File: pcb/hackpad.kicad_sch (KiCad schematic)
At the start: 31 parts, among them U1 XIAO-RP2040-SMD

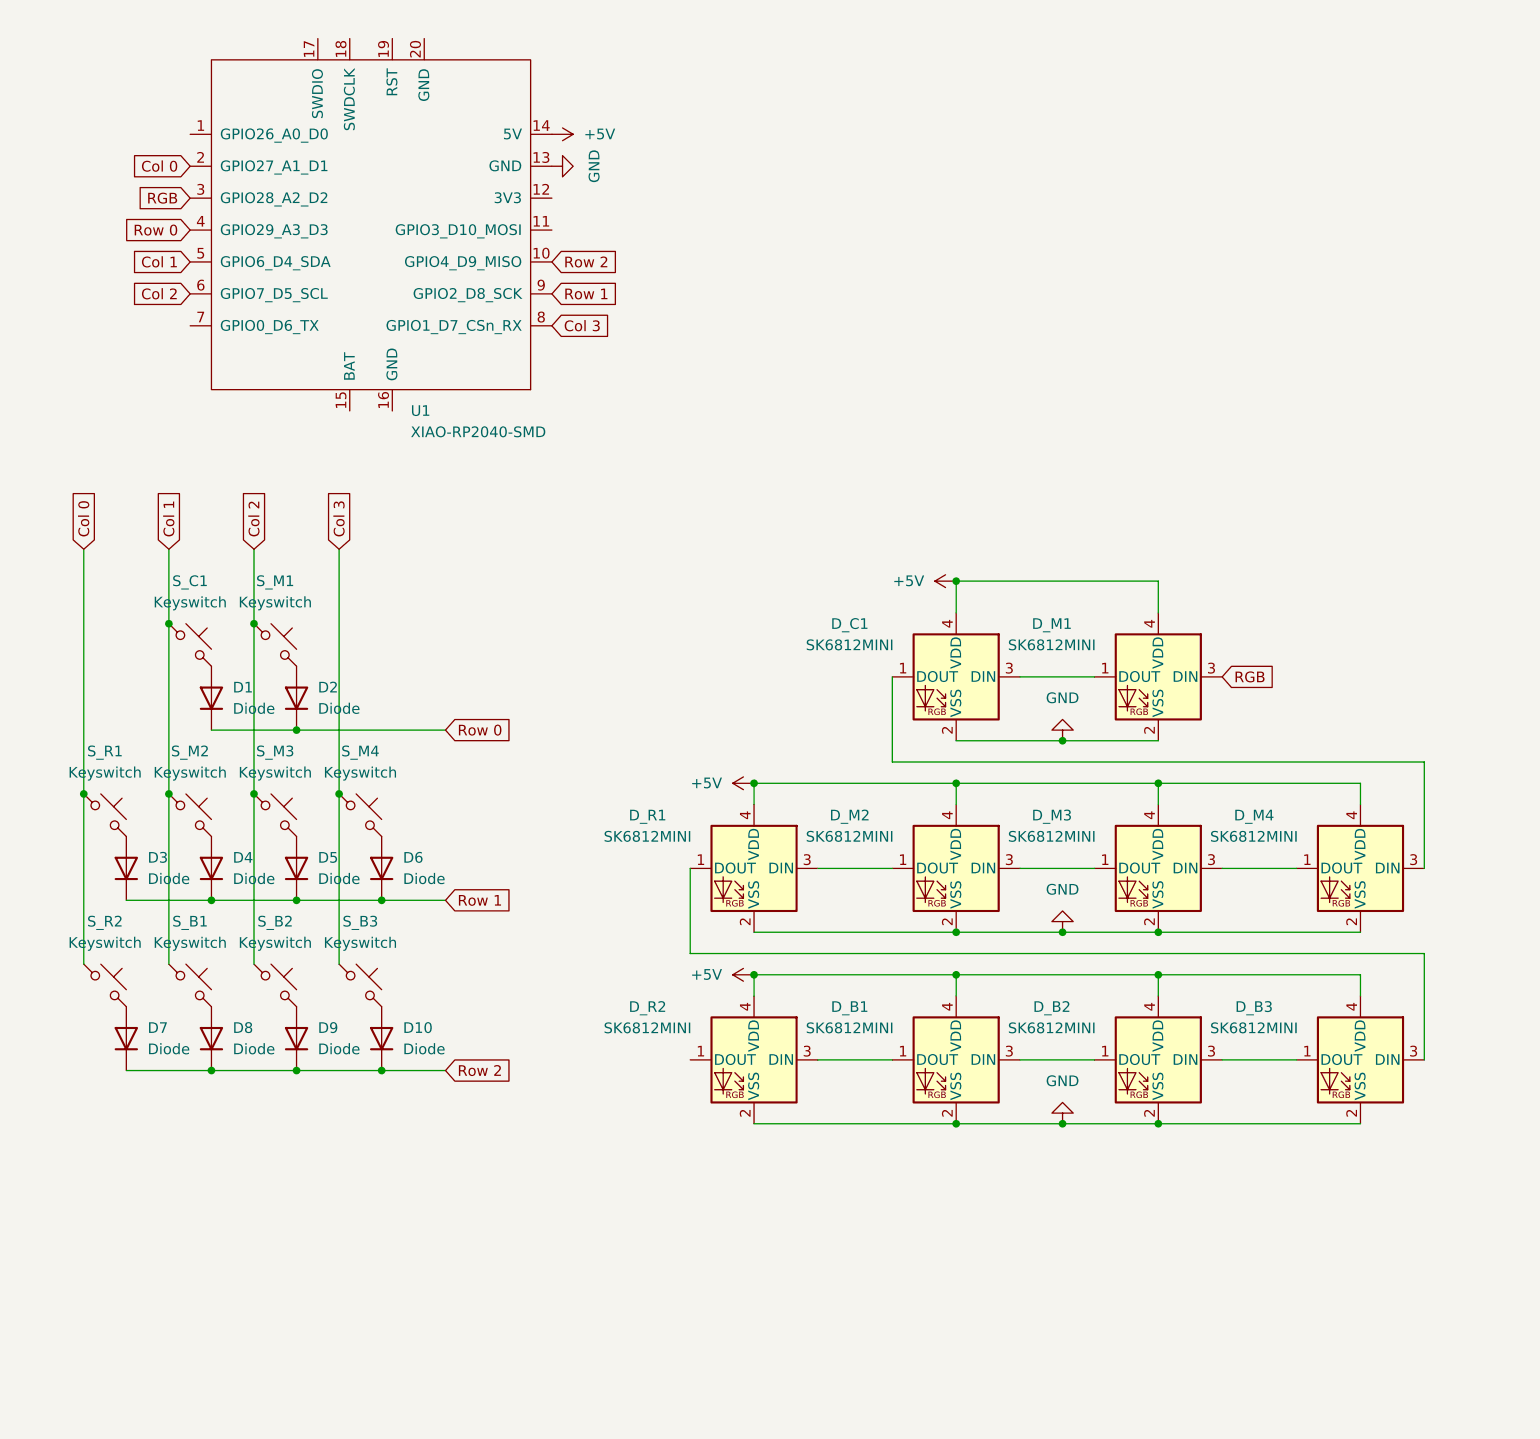
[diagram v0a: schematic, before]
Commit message: i used the wrong data sheet to edit the footprint, changed the pcb to actually work :(
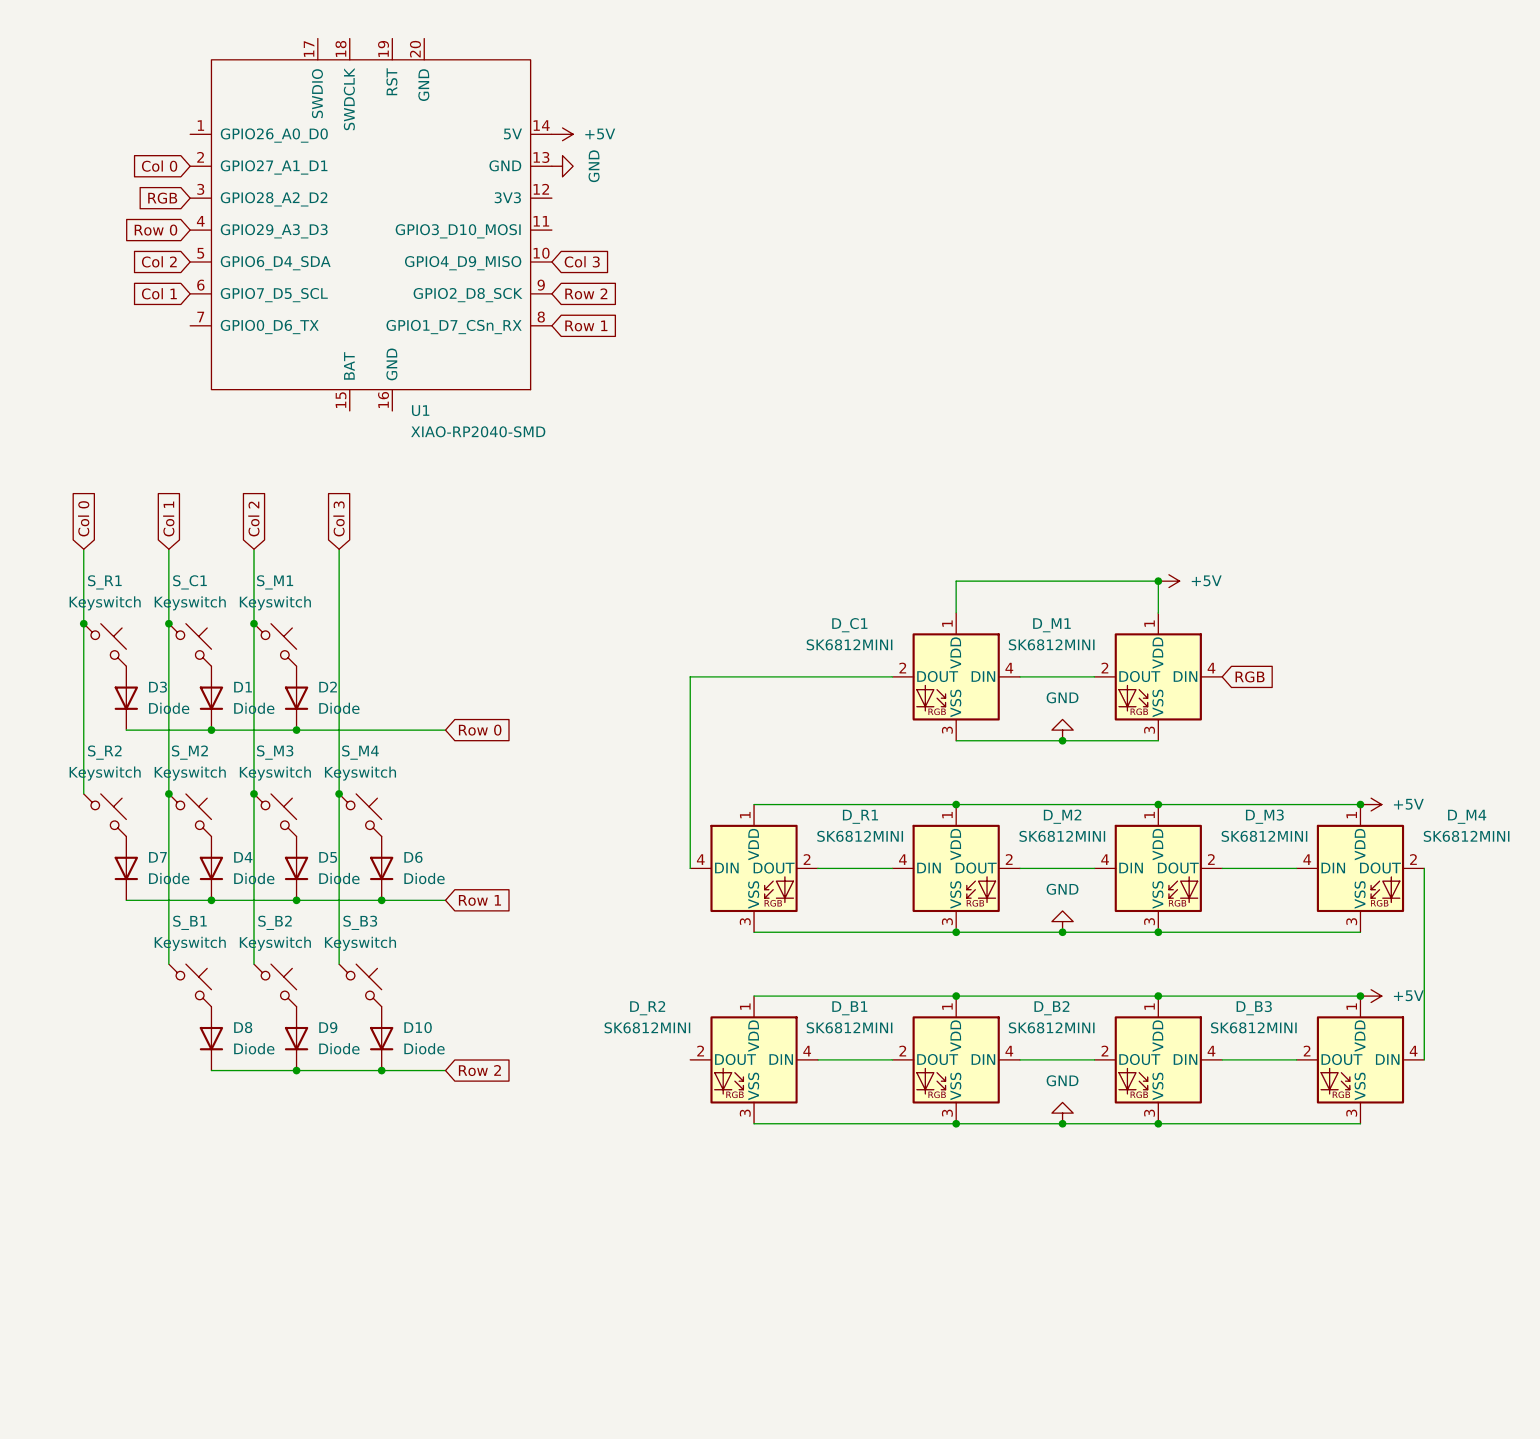
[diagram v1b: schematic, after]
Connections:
- net +5V: now also D_B1.1 (VDD), D_B2.1 (VDD), D_B3.1 (VDD), D_C1.1 (VDD), D_M1.1 (VDD), D_M2.1 (VDD), D_M3.1 (VDD), D_M4.1 (VDD), D_R1.1 (VDD), D_R2.1 (VDD); no longer D_B1.4 (VDD), D_B2.4 (VDD), D_B3.4 (VDD), D_C1.4 (VDD), D_M1.4 (VDD), D_M2.4 (VDD), D_M3.4 (VDD), D_M4.4 (VDD), D_R1.4 (VDD), D_R2.4 (VDD)
- net Col 1: now also U1.6 (GPIO7_D5_SCL); no longer U1.5 (GPIO6_D4_SDA)
- net Col 2: now also U1.5 (GPIO6_D4_SDA); no longer U1.6 (GPIO7_D5_SCL)
- net Col 3: now also U1.10 (GPIO4_D9_MISO); no longer U1.8 (GPIO1_D7_CSn_RX)
- net GND: now also D_B1.3 (VSS), D_B2.3 (VSS), D_B3.3 (VSS), D_C1.3 (VSS), D_M1.3 (VSS), D_M2.3 (VSS), D_M3.3 (VSS), D_M4.3 (VSS), D_R1.3 (VSS), D_R2.3 (VSS); no longer D_B1.2 (VSS), D_B2.2 (VSS), D_B3.2 (VSS), D_C1.2 (VSS), D_M1.2 (VSS), D_M2.2 (VSS), D_M3.2 (VSS), D_M4.2 (VSS), D_R1.2 (VSS), D_R2.2 (VSS)
- net RGB: now also D_M1.4 (DIN); no longer D_M1.3 (DIN)
- net Row 0: now also D3.1 (K)
- net Row 1: now also D7.1 (K), U1.8 (GPIO1_D7_CSn_RX); no longer D3.1 (K), U1.9 (GPIO2_D8_SCK)
- net Row 2: now also U1.9 (GPIO2_D8_SCK); no longer D7.1 (K), U1.10 (GPIO4_D9_MISO)
- new net: D_C1.4 (DIN), D_M1.2 (DOUT)
- new net: D_B2.4 (DIN), D_B3.2 (DOUT)
- new net: D_B3.4 (DIN), D_M4.2 (DOUT)
- new net: D_B1.4 (DIN), D_B2.2 (DOUT)
- new net: D_B1.2 (DOUT), D_R2.4 (DIN)
- new net: D_M2.4 (DIN), D_R1.2 (DOUT)
- new net: D_C1.2 (DOUT), D_R1.4 (DIN)
- new net: D_M3.2 (DOUT), D_M4.4 (DIN)
- new net: D_M2.2 (DOUT), D_M3.4 (DIN)
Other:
- moved on the sheet: D3, D7, S_R1, S_R2

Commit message: make erc happy
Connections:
- no-connect marks 0 -> 11

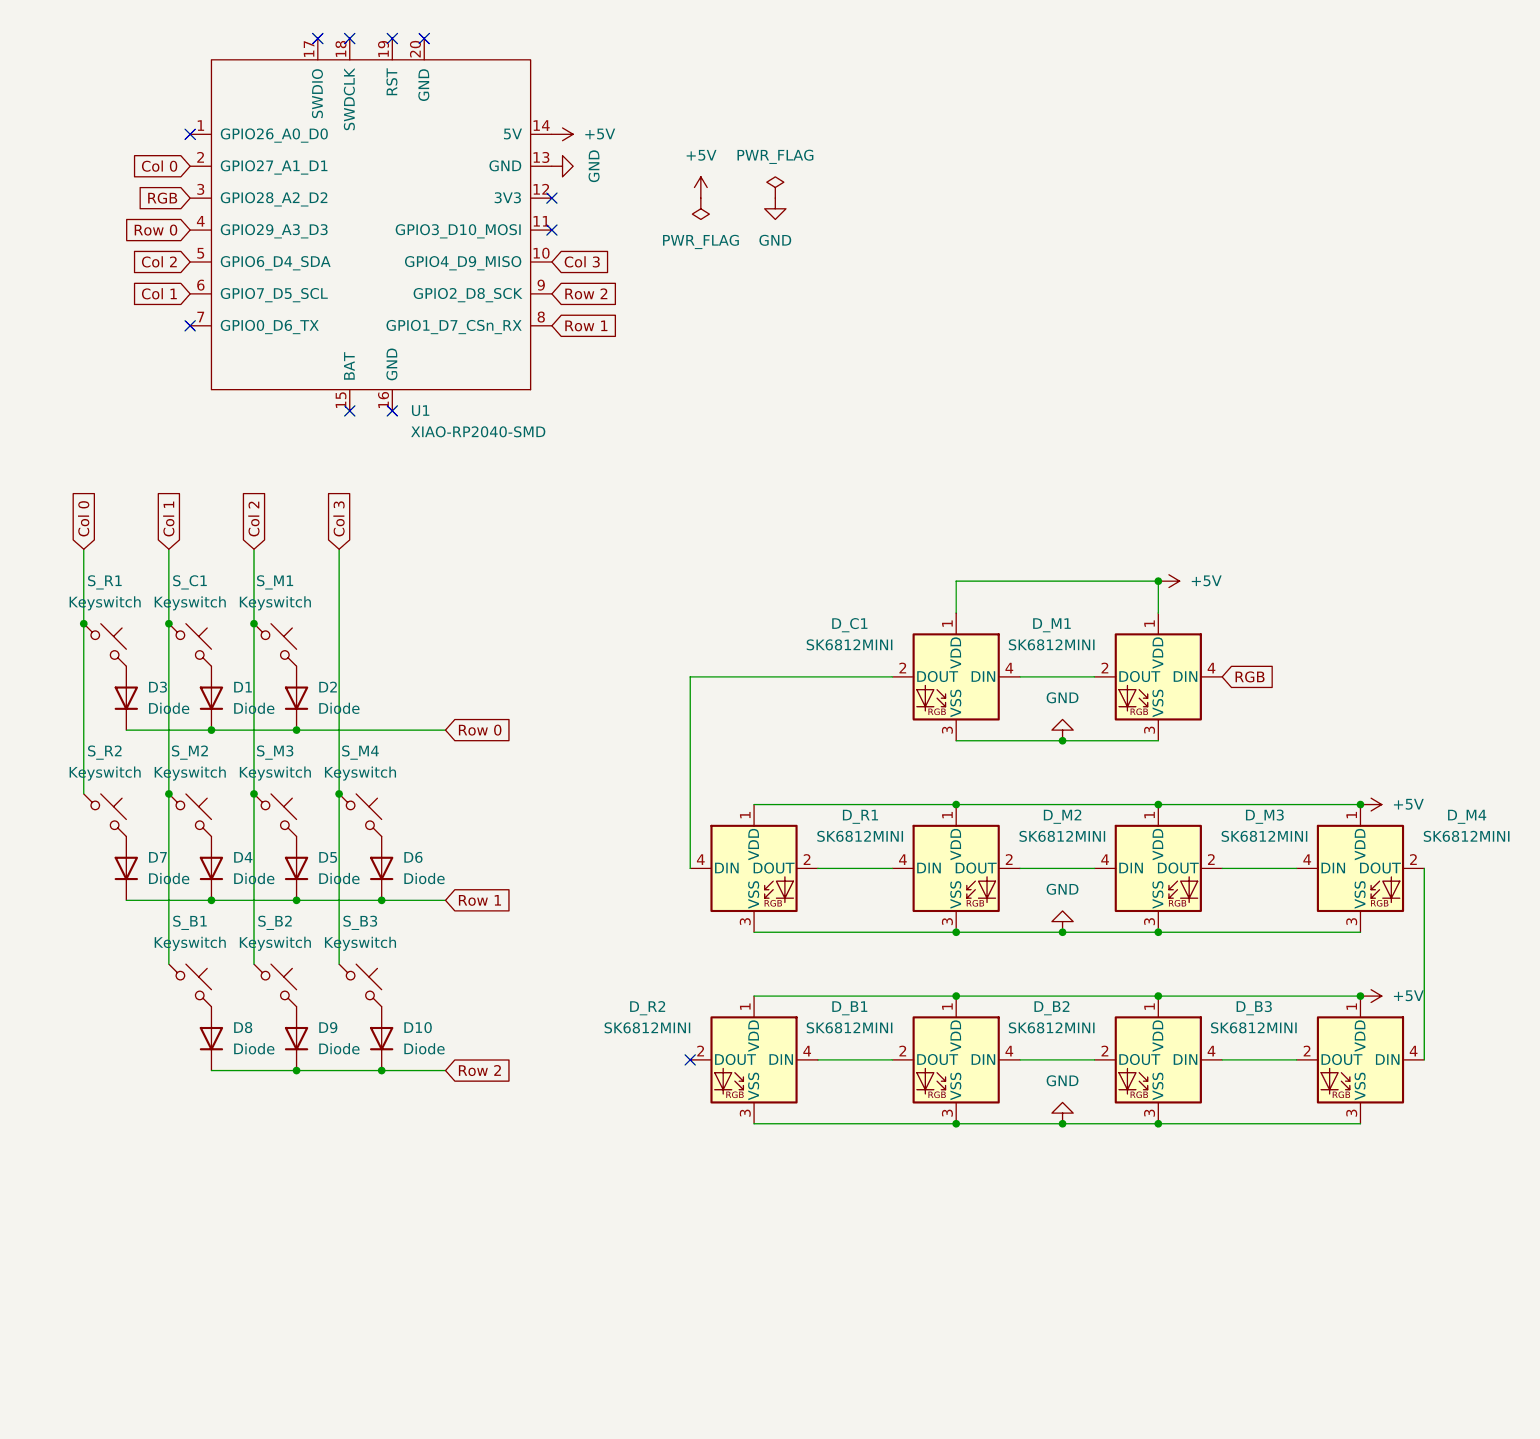
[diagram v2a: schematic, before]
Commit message: add holes to the smd debug pads
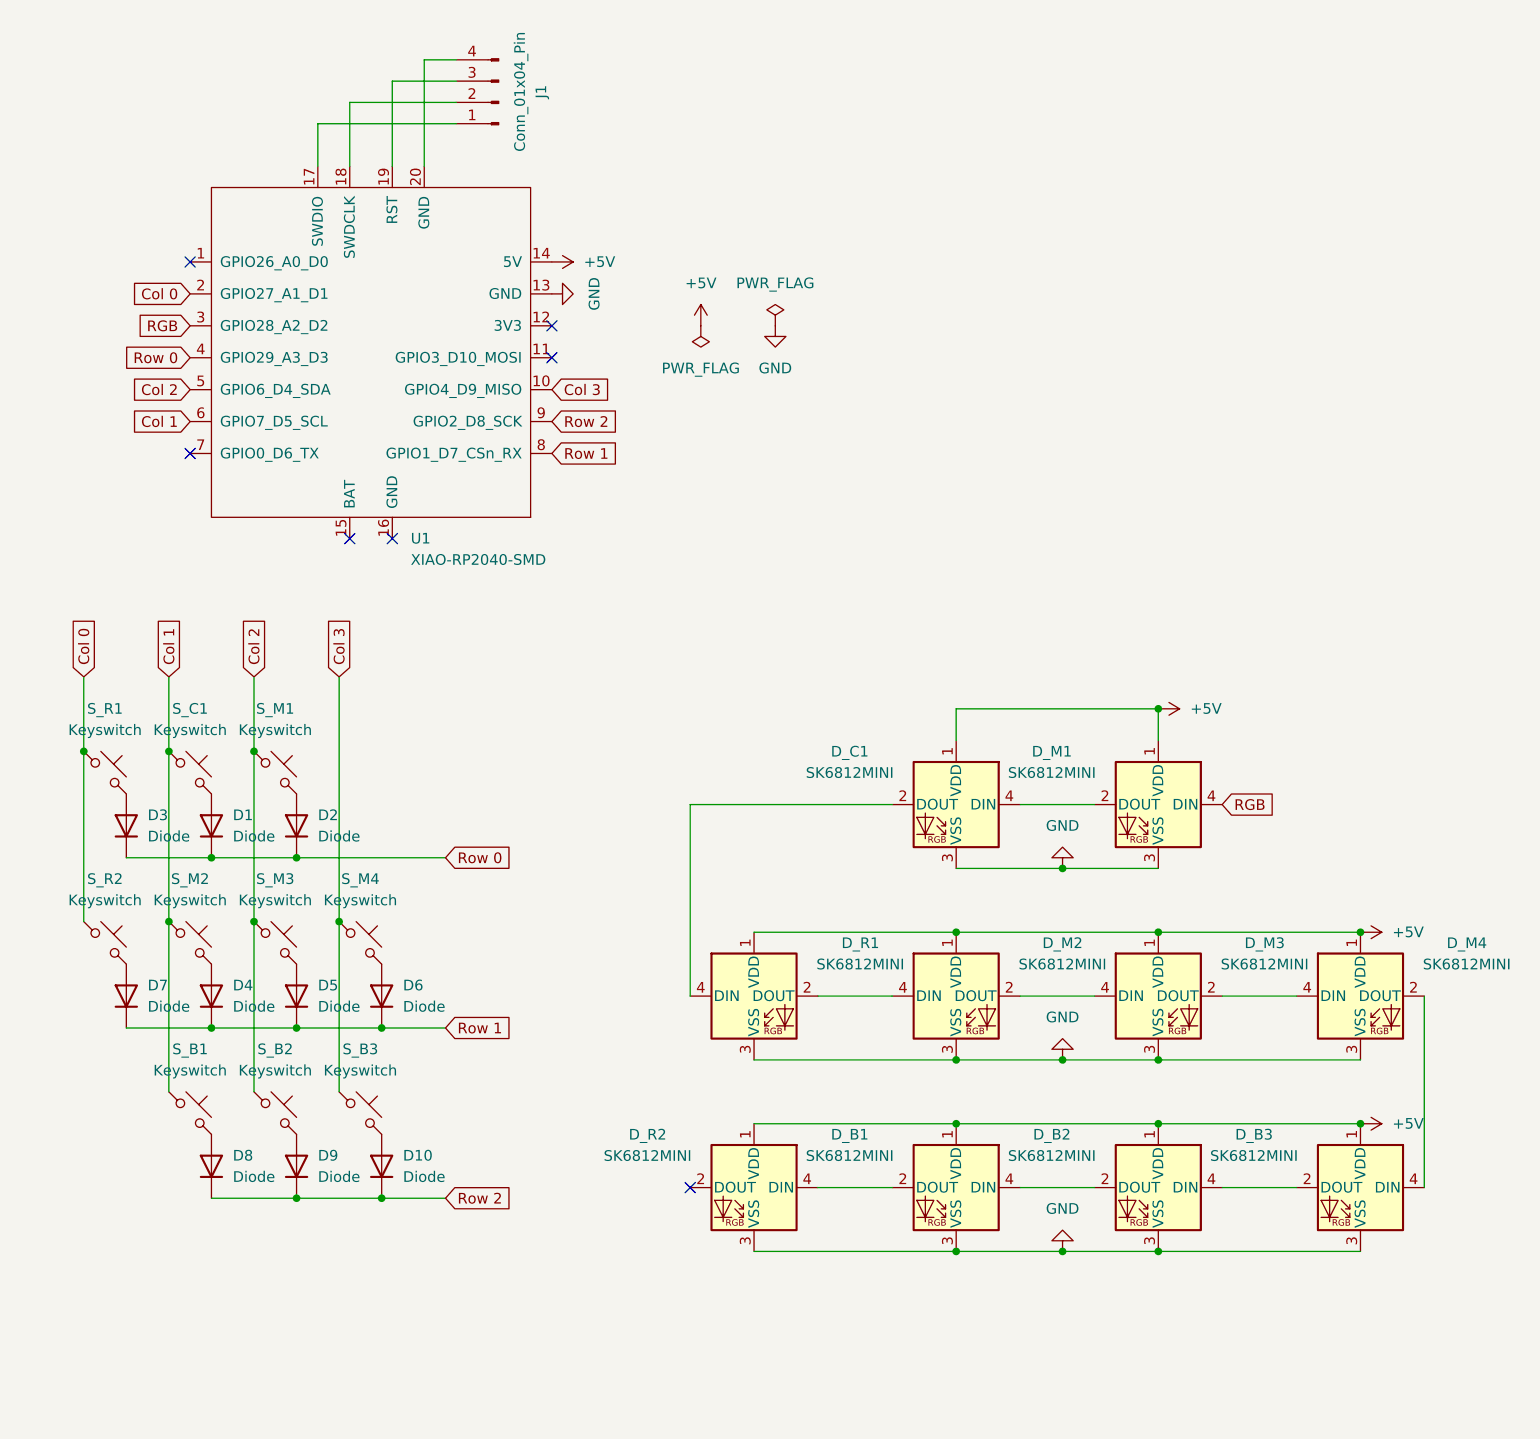
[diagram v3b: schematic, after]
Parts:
- added J1: Conn_01x04_Pin, Connector_PinHeader_1.00mm:PinHeader_1x04_P1.00mm_Horizontal, symbol Connector:Conn_01x04_Pin
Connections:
- net at U1.17 (SWDIO): now also J1.1 (Pin_1)
- net at U1.18 (SWDCLK): now also J1.2 (Pin_2)
- net at U1.19 (RST): now also J1.3 (Pin_3)
- net at U1.20 (GND): now also J1.4 (Pin_4)
- no-connect marks 11 -> 7
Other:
- moved on the sheet: D1, D10, D2, D3, D4, D5, D6, D7, D8, D9, D_B1, D_B2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
